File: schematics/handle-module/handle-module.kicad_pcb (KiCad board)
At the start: 4 copper layers, 80 x 42 mm, 114 parts, among them J1 2*LiFePo4@18650@1800mAh, 6,4V, J2 Charger, J3 USBASP, Q1 IRLML5203, Q10 IRLML0030, Q11 IRLML0030, Q2 IRLML5203, Q3 IRLML0030, Q4 IRLML0030, Q5 IRLML0030, Q6 IRLML5203, Q7 IRLML0030, Q8 IRLML0030, Q9 IRLML0030, SW1 KLS7-TS3601-5.0-180, SW2 KLS7-TS3601-5.0-180, U1 STX882@443MHz, U2 SRX882@443MHz, U3 ATmega328-A, U4 AMS1117-5.0, U5 BQ24780S, U7 INA219, X1 HC-49U, 8MHz

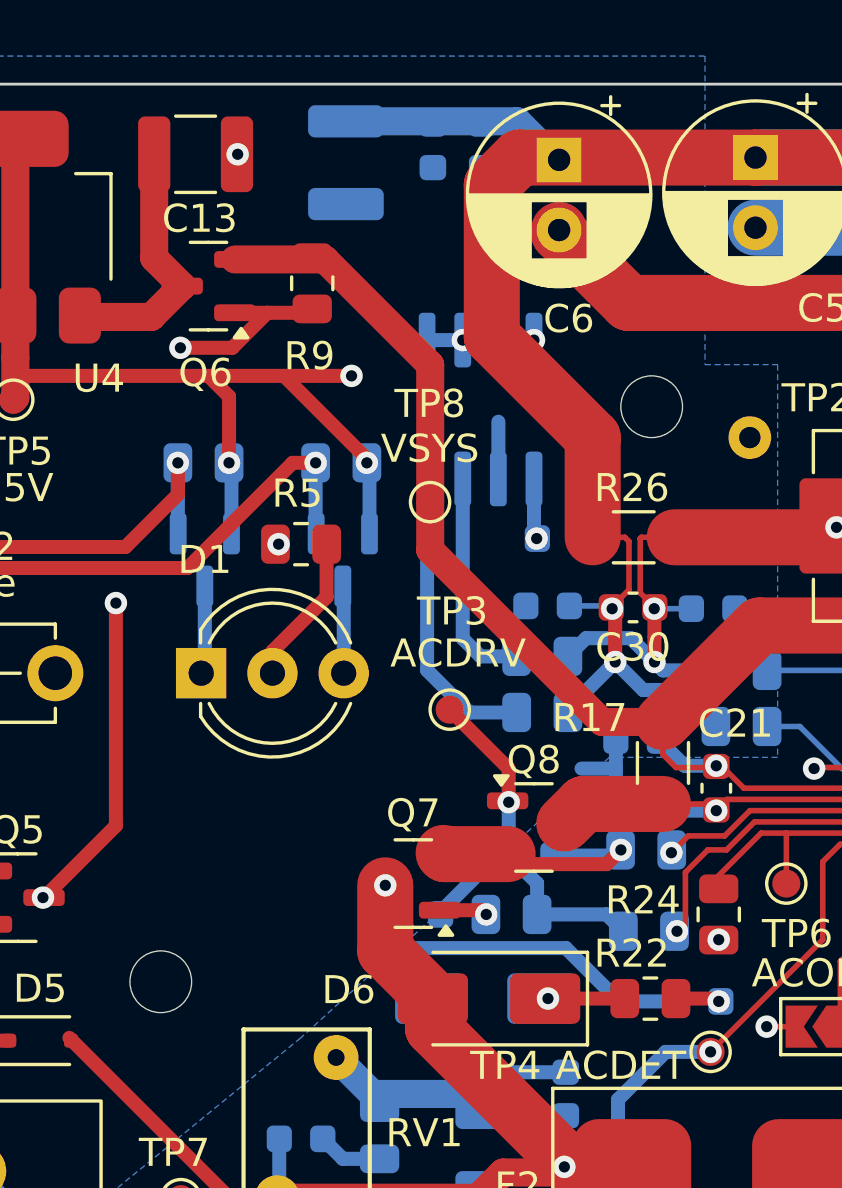
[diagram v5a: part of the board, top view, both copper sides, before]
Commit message: removed blind vias - it's production is too expensive
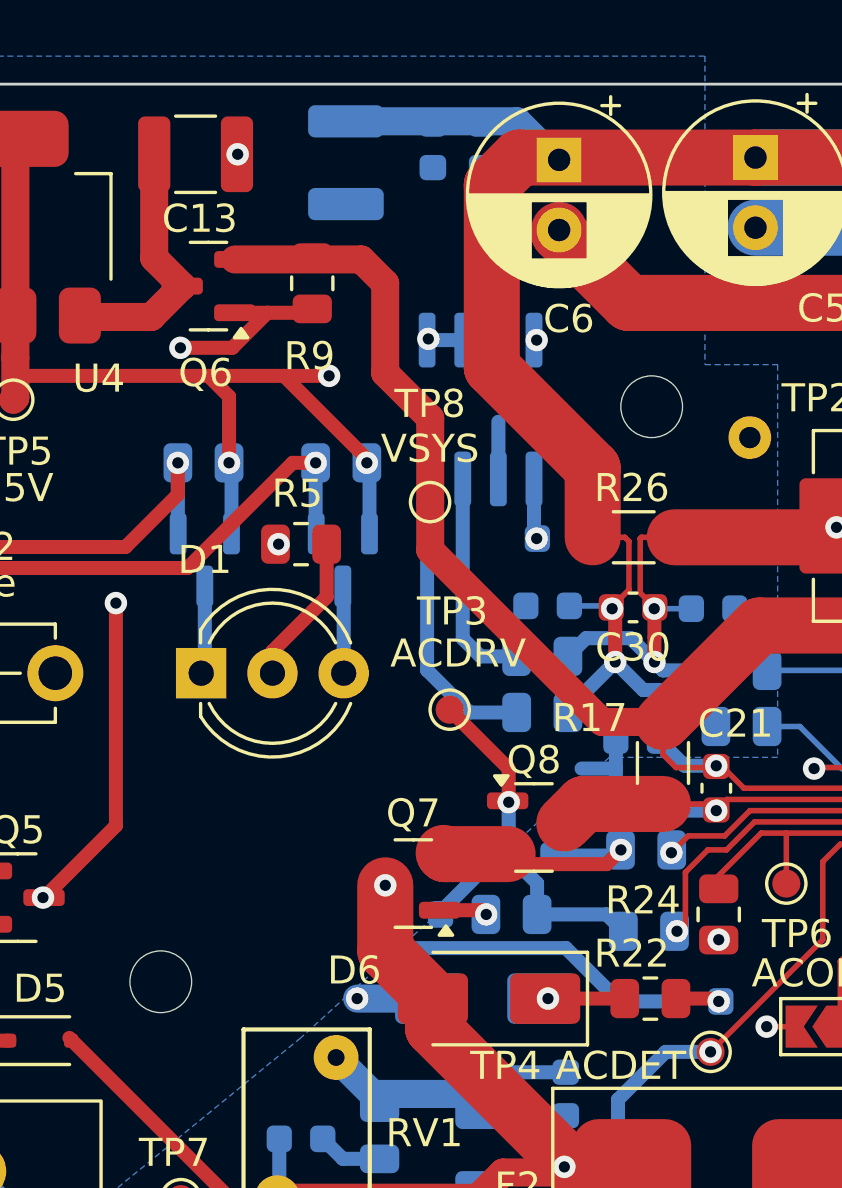
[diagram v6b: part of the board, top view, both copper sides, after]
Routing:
- net /VSYS: track 65.1 -> 65.9 mm
- net /SDA: track 95.2 -> 94.7 mm
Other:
- board text added: "ACW-handle-v1.2.1"
- board text removed: "ACW-handle-v1.2"
